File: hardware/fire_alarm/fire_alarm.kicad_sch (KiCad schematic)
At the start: 0 parts

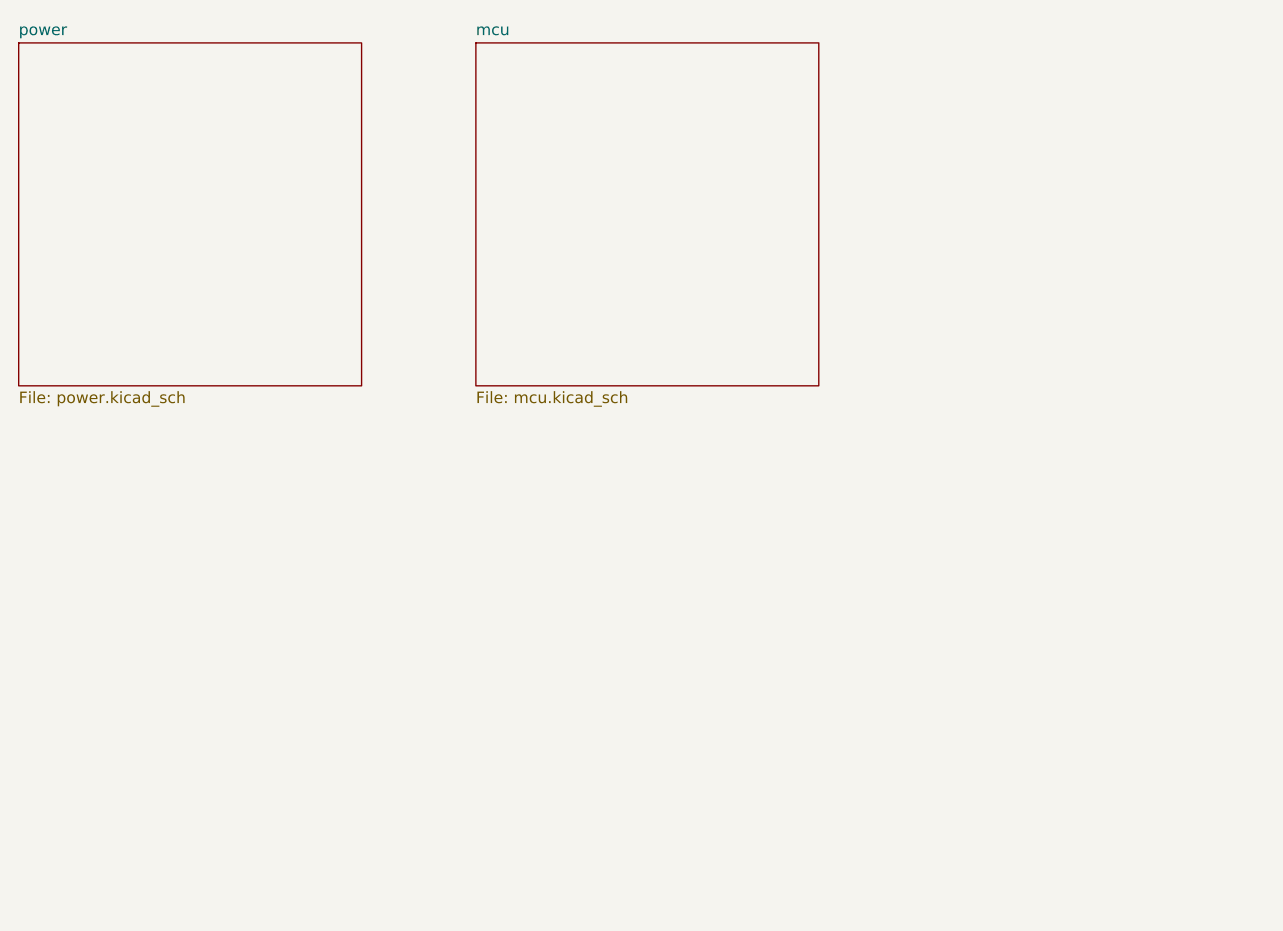
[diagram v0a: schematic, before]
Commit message: feat: update schematic sensors, ui
Signed-off-by: Trung Hieu Nguyen <hieu.nguyenarc03@gmail.com>
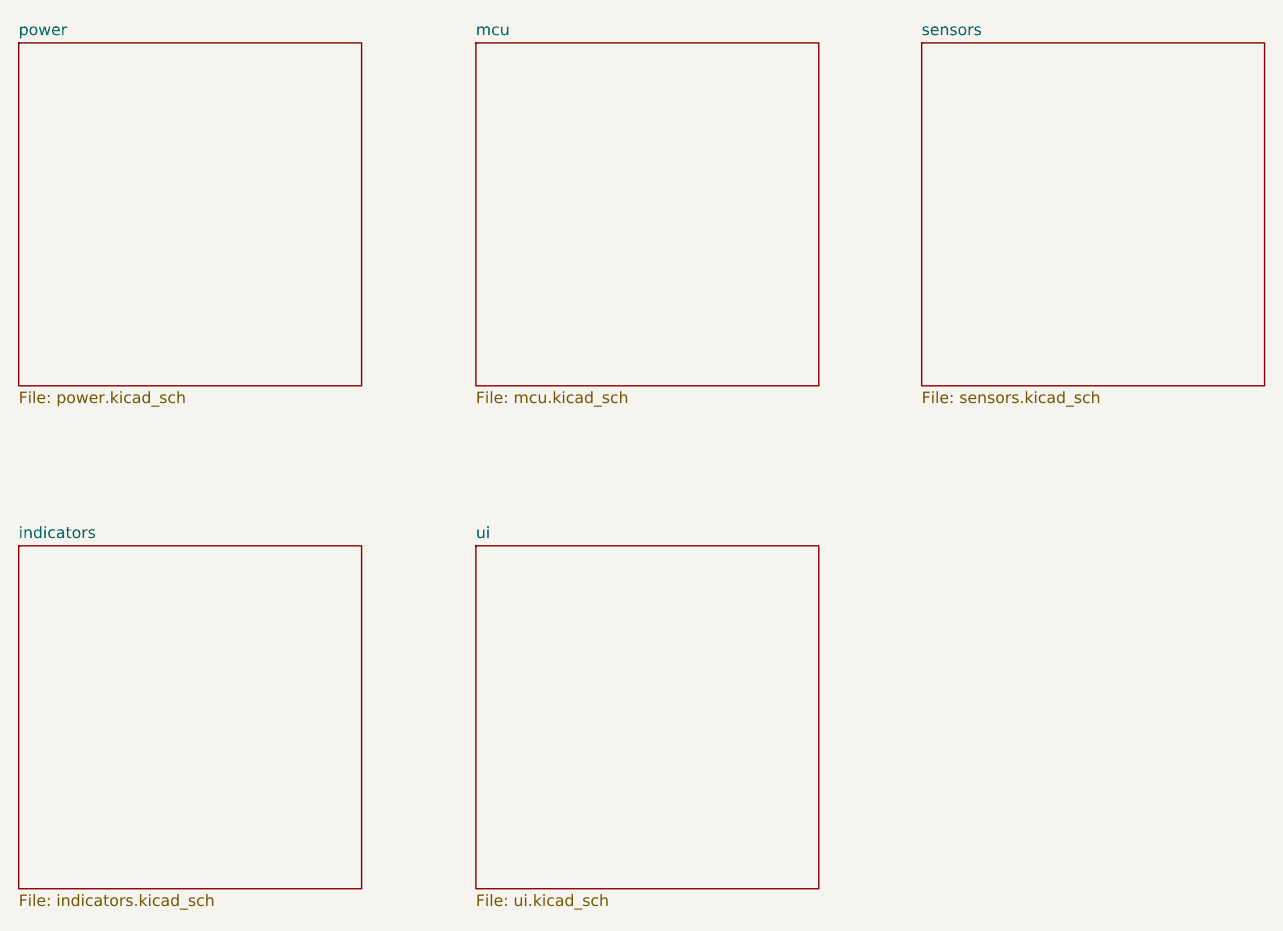
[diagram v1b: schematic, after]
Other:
- added sheet indicators (indicators.kicad_sch)
- added sheet sensors (sensors.kicad_sch)
- added sheet ui (ui.kicad_sch)
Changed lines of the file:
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@@
+	)
+	(sheet
+		(at 127 106.68)
+		(size 38.1 38.1)
+		(exclude_from_sim no)
+		(in_bom yes)
+		(on_board yes)
+		(dnp no)
+		(fields_autoplaced yes)
+		(stroke
+			(width 0.1524)
+			(type solid)
+		)
+		(fill
+			(color 0 0 0 0.0000)
+		)
+		(property "Sheetname" "ui"
+			(at 127 105.9684 0)
+			(effects
+				(font
+					(size 1.27 1.27)
+				)
+				(justify left bottom)
+			)
+		)
+		(property "Sheetfile" "ui.kicad_sch"
+			(at 127 145.3646 0)
+			(effects
+				(font
+					(size 1.27 1.27)
+				)
+				(justify left top)
+			)
+		)
+		(instances
+			(project "fire_alarm"
+				(path "/0ad2965f-ac4e-45fe-9d64-44da87c25aaa"
+					(page "6")
+				)
+			)
+		)
+	)
+	(sheet
+		(at 76.2 106.68)
+		(size 38.1 38.1)
+		(exclude_from_sim no)
+		(in_bom yes)
+		(on_board yes)
+		(dnp no)
+		(fields_autoplaced yes)
+		(stroke
+			(width 0.1524)
+			(type solid)
+		)
+		(fill
+			(color 0 0 0 0.0000)
+		)
+		(property "Sheetname" "indicators"
+			(at 76.2 105.9684 0)
+			(effects
+				(font
+					(size 1.27 1.27)
+				)
+				(justify left bottom)
+			)
+		)
+		(property "Sheetfile" "indicators.kicad_sch"
+			(at 76.2 145.3646 0)
+			(effects
+				(font
+					(size 1.27 1.27)
+				)
+				(justify left top)
+			)
+		)
+		(instances
+			(project "fire_alarm"
+				(path "/0ad2965f-ac4e-45fe-9d64-44da87c25aaa"
+					(page "5")
+				)
+			)
+		)
+	)
+	(sheet
+		(at 176.53 50.8)
+		(size 38.1 38.1)
+		(exclude_from_sim no)
+		(in_bom yes)
+		(on_board yes)
+		(dnp no)
+		(fields_autoplaced yes)
+		(stroke
+			(width 0.1524)
+			(type solid)
+		)
+		(fill
+			(color 0 0 0 0.0000)
+		)
+		(property "Sheetname" "sensors"
+			(at 176.53 50.0884 0)
+			(effects
+				(font
+					(size 1.27 1.27)
+				)
+				(justify left bottom)
+			)
+		)
+		(property "Sheetfile" "sensors.kicad_sch"
+			(at 176.53 89.4846 0)
+			(effects
+				(font
+					(size 1.27 1.27)
+				)
+				(justify left top)
+			)
+		)
+		(instances
+			(project "fire_alarm"
+				(path "/0ad2965f-ac4e-45fe-9d64-44da87c25aaa"
+					(page "4")
+				)
+			)
+		)
 	)
 	(sheet
